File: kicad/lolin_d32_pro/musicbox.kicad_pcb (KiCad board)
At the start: 2 copper layers, 97.3 x 49 mm, 7 parts

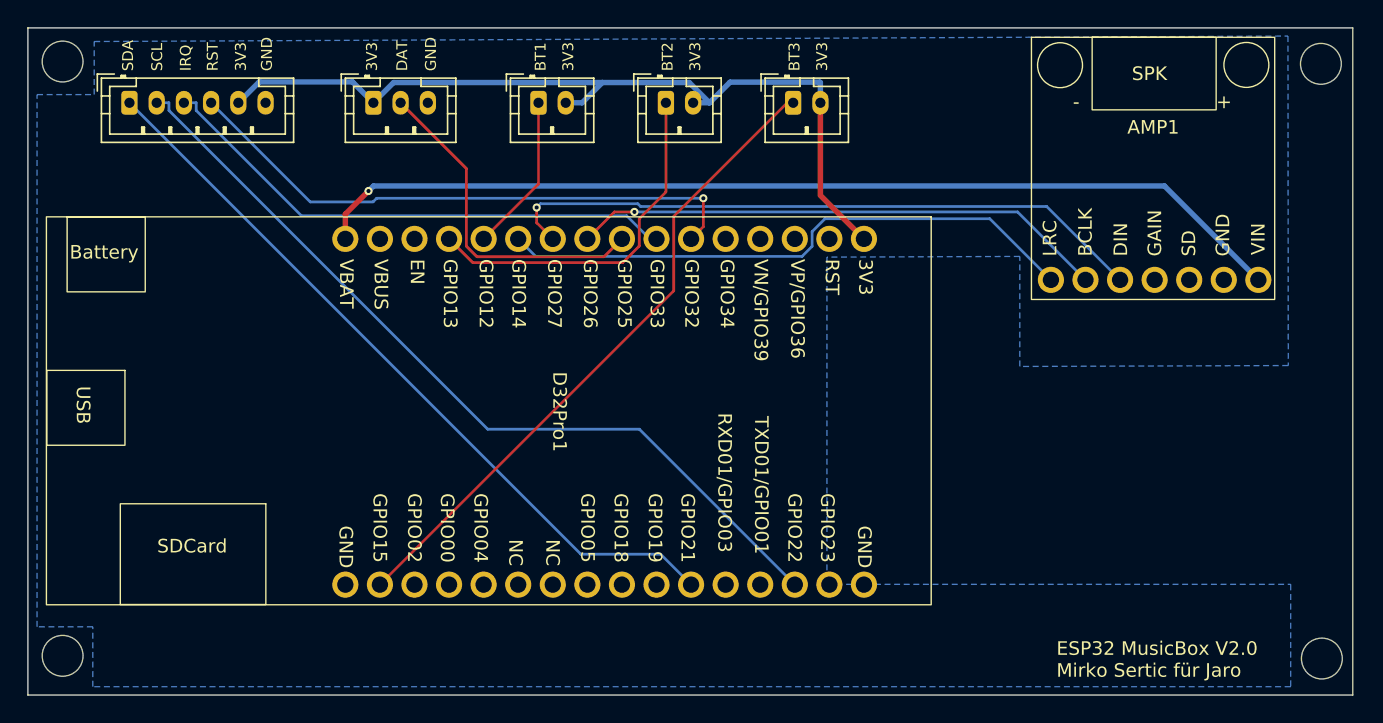
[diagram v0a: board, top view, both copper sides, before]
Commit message: Working on Bluetooth Speaker mode
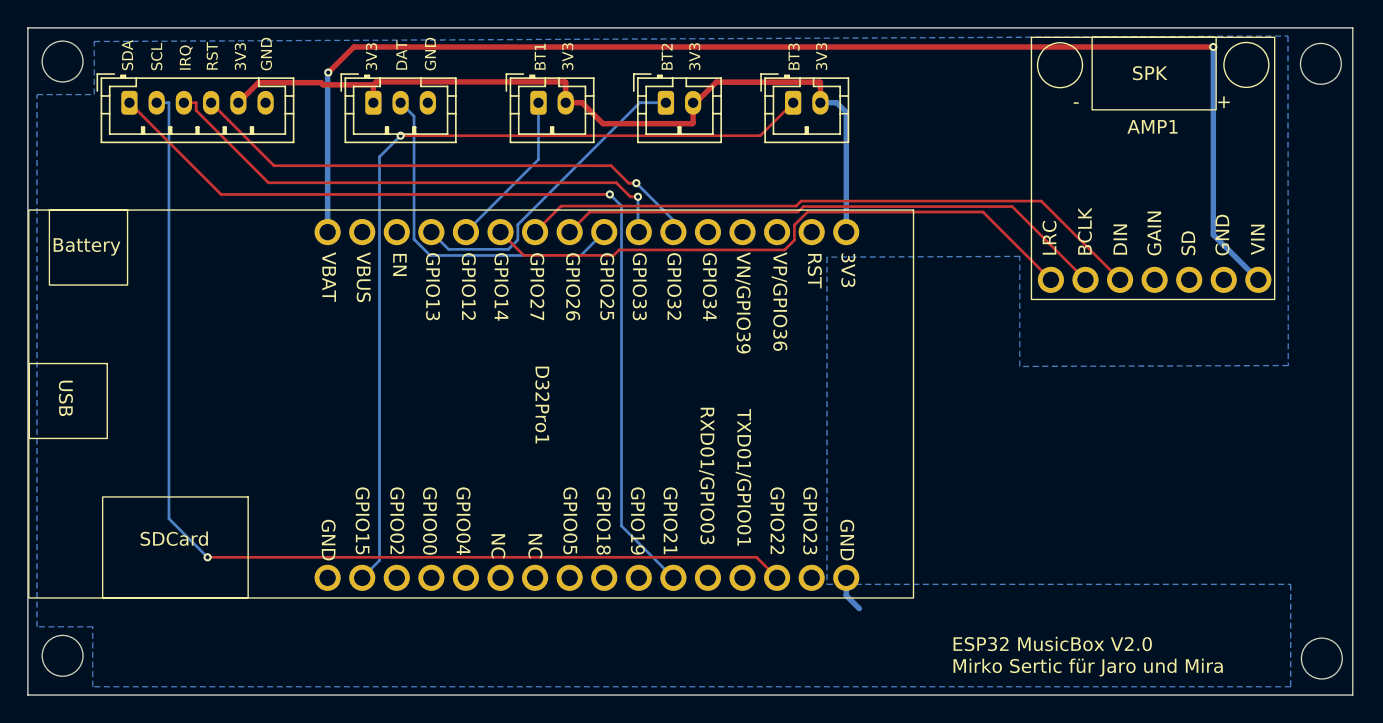
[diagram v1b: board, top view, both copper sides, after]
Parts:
- moved D32Pro1 1.39 mm to (127.4, 60.7)
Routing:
- net VBAT: track 72.6 -> 96.0 mm, vias 1 -> 2
- net /I2C_SCL: track 61.9 -> 77.9 mm, vias 0 -> 1
- net /BT3: track 48.2 -> 63.5 mm, vias 0 -> 1
- net /I2C_SDA: track 55.9 -> 68.2 mm, vias 0 -> 1
- net /RFID_RST: track 42.6 -> 38.4 mm
- net /BT2: track 26.5 -> 22.9 mm
- net GND: track 0.00 -> 2.66 mm
- net /I2S_WS: track 43.3 -> 45.2 mm
- net /I2S_DIN: track 48.1 -> 46.3 mm, vias 1 -> 0
- net 3V3: track 63.2 -> 61.7 mm
- net /I2S_BCK: track 39.5 -> 40.9 mm, vias 1 -> 0
- net /ADR_LED: track 24.8 -> 25.6 mm
- net /RFID_IRQ: vias 0 -> 1
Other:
- board text added: "ESP32 MusicBox V2.0 Mirko Sertic für Jaro und Mira"
- board text removed: "ESP32 MusicBox V2.0 Mirko Sertic für Jaro"

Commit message: Updated Gerbers for Lolin D32 Pro
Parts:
- moved D32Pro1 5.07 mm to (125.3, 56.1)
- moved BT3Con1 4.75 mm to (151.1, 38.9)
- moved BT1Con1 4.75 mm to (132.4, 38.9)
- moved BT2Con1 4.75 mm to (141.7, 38.9)
- moved NeoPixelCon1 4.75 mm to (120.2, 38.9)
- moved RFIDCon1 4.75 mm to (102.3, 38.9)
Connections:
- NeoPixelCon1 pad 1: 3V3 -> VBAT
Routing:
- net GND: track 2.66 -> 130.5 mm, vias 0 -> 1
- net /ADR_LED: track 25.6 -> 11.2 mm
- net /I2C_SCL: track 77.9 -> 65.1 mm
- net /I2C_SDA: track 68.2 -> 58.3 mm
- net VBAT: track 96.0 -> 86.5 mm, vias 2 -> 1
- net /RFID_IRQ: track 39.2 -> 31.7 mm, vias 1 -> 0
- net /BT1: track 11.7 -> 18.7 mm
- net 3V3: track 61.7 -> 55.9 mm
- net /RFID_RST: track 38.4 -> 32.6 mm
- net /I2S_WS: track 45.2 -> 50.4 mm, vias 0 -> 1
- net /BT3: track 63.5 -> 59.8 mm
- net /BT2: track 22.9 -> 26.3 mm, vias 0 -> 1
- net /I2S_DIN: track 46.3 -> 48.8 mm
- net /I2S_BCK: track 40.9 -> 43.4 mm
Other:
- board size 97.3 x 49 mm -> 97.3 x 40.7 mm
- board text added: "VBAT"
